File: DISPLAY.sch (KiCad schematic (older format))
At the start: 37 parts, among them P301 SEPS525, U302 TPS61041DBV

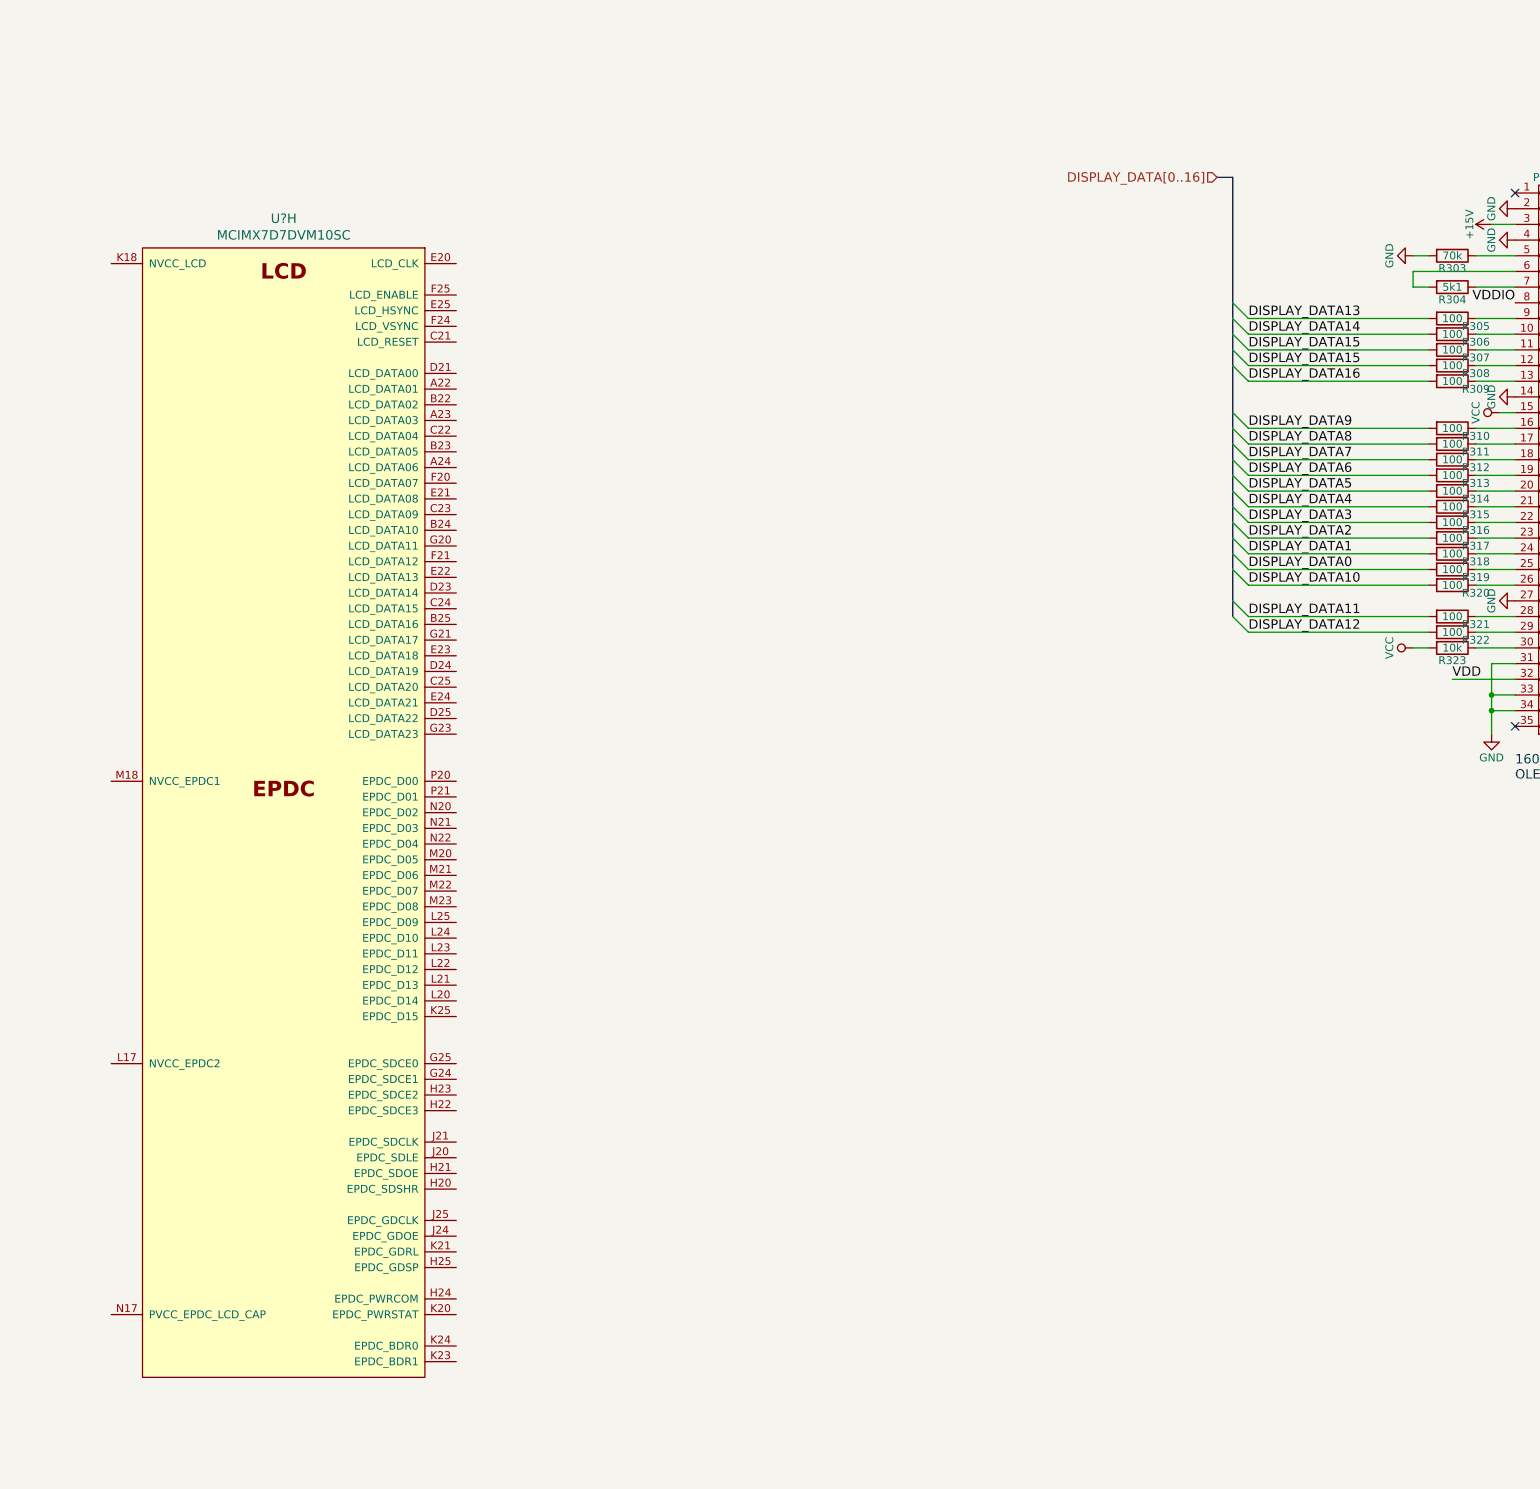
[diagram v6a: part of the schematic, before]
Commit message: Added SD card, eMMC, Display
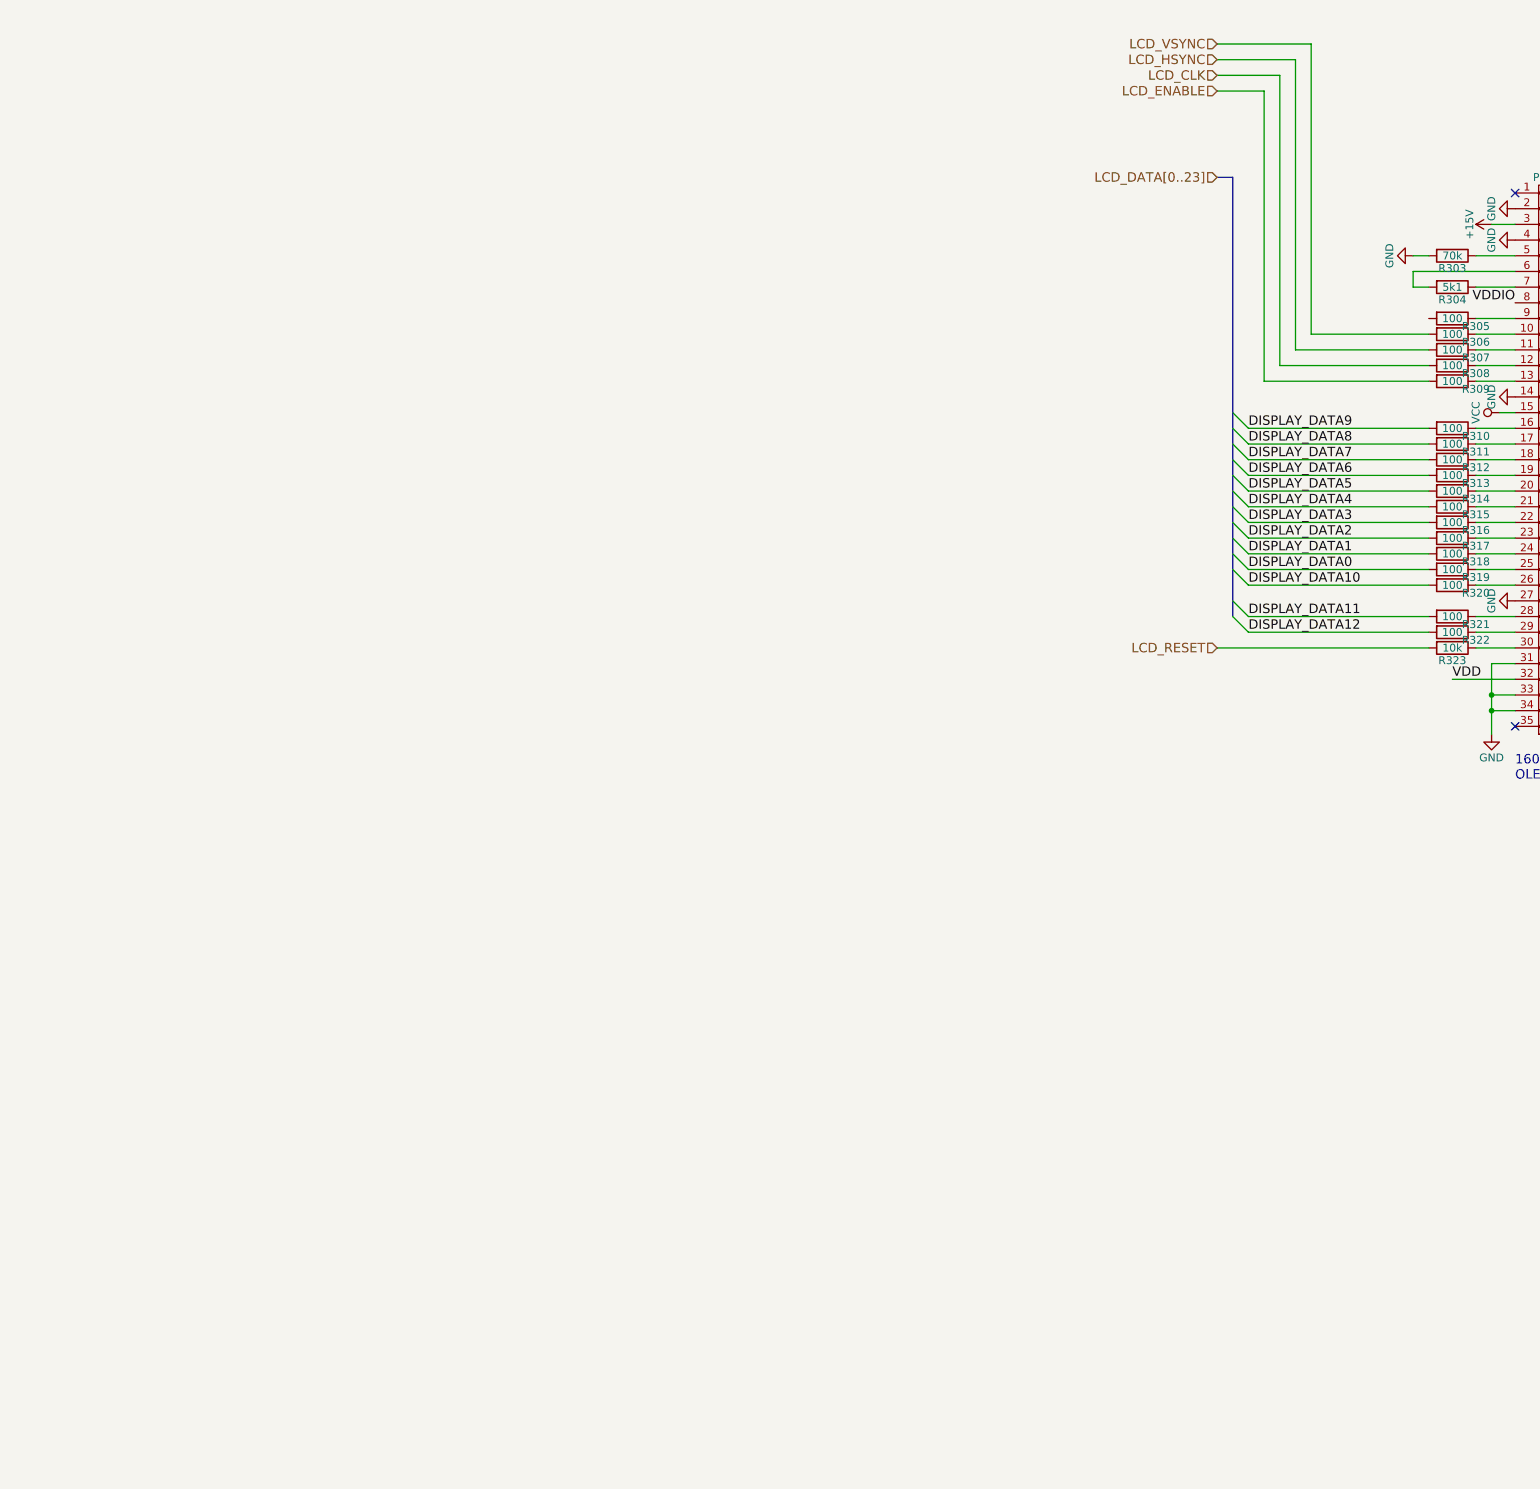
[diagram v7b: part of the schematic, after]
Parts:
- removed U?: MCIMX7D7DVM10SC, symbol MCIMX7D7DVM10SC
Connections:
- net VCC: no longer R323.2
- net DISPLAY_DATA13: no longer names the net of R305.2
- net DISPLAY_DATA14 renamed LCD_VSYNC
- net DISPLAY_DATA15 renamed LCD_CLK
- net LCD_CLK: no longer R307.2
- net DISPLAY_DATA16 renamed LCD_ENABLE
- new net LCD_HSYNC: R307.2
- new net LCD_RESET: R323.2
